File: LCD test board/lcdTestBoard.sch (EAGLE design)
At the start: 71 parts, among them CON2 AXE534124, U1 LP2980-ADJ, U2 ST2378E_TSSOP, U3 MCP1662, U4 TPS62260, U5 ST2378E_TSSOP, U6 LP2980-ADJ, U7 TPS62260, U8 LP2980-ADJ, U9 TPS62260

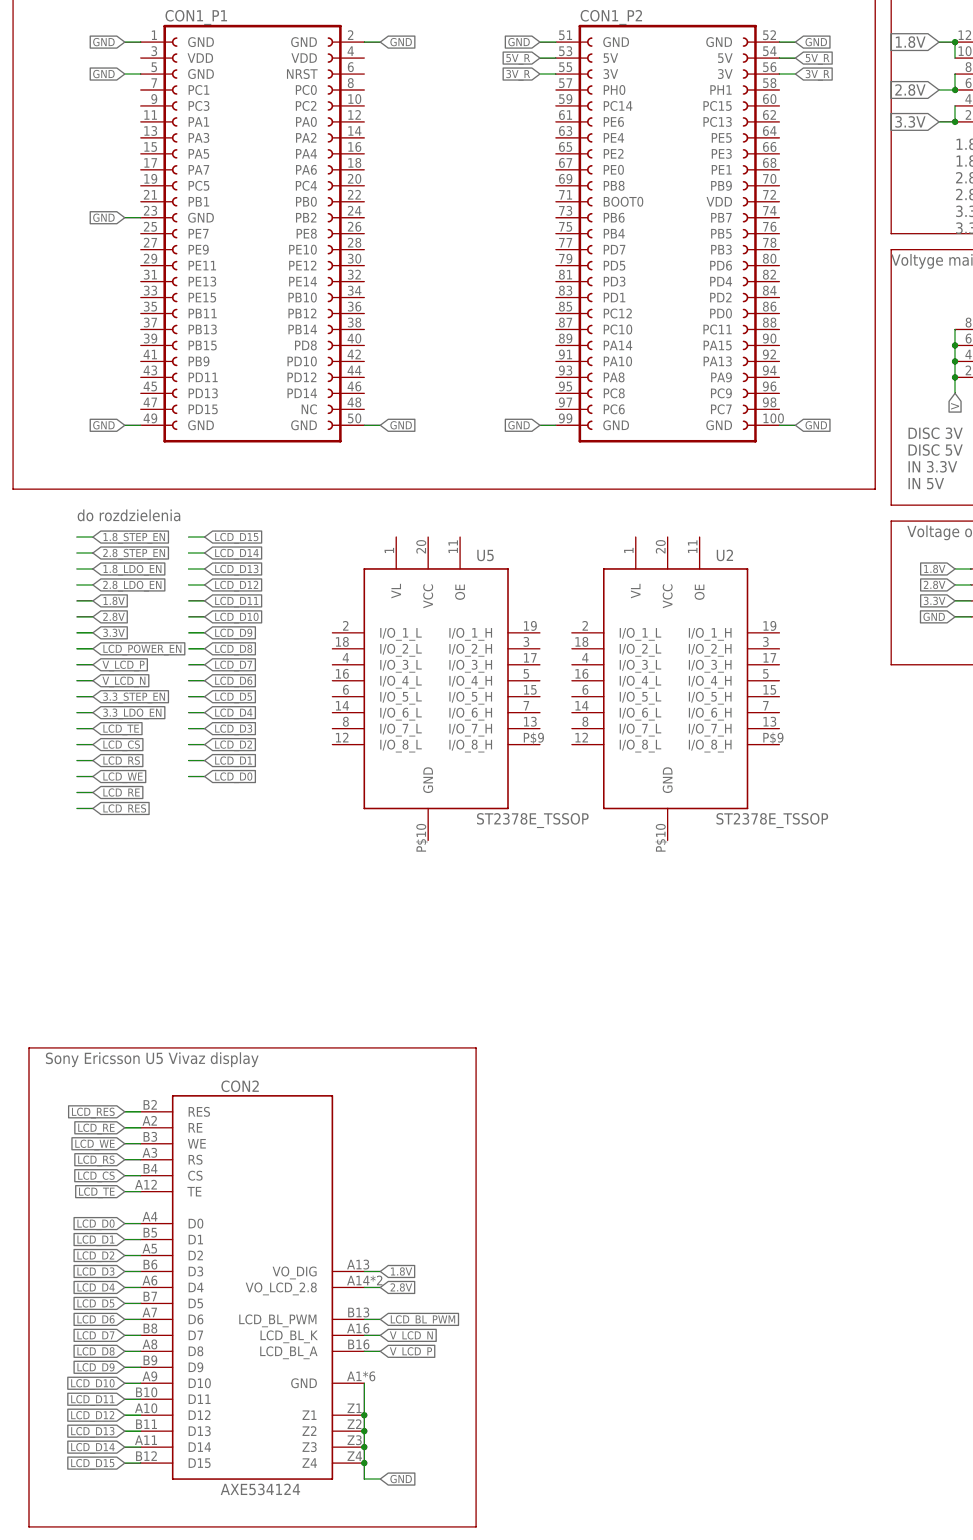
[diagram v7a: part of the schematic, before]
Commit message: polaczono piny od lcd
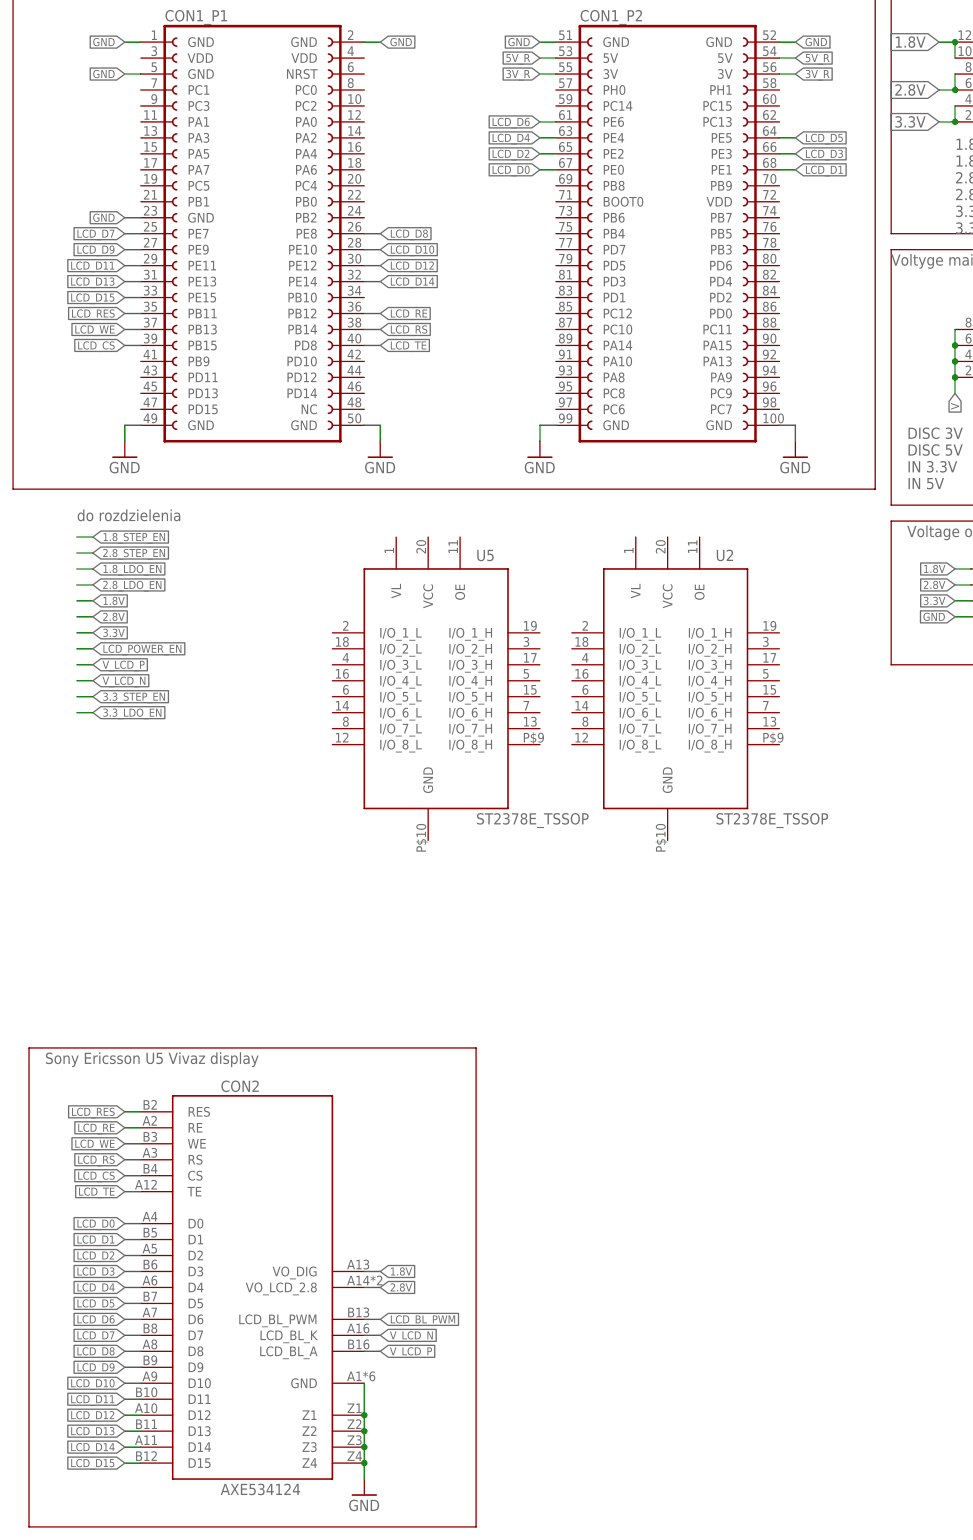
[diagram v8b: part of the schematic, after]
